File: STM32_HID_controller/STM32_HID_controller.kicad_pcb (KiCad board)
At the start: 2 copper layers, 237.3 x 103.7 mm, 49 parts, among them J1 USB_B_Micro, J2 Conn_01x04_Pin, J3 Conn_01x03_Pin, J5 Conn_01x03_Pin, SW1 SW_SPDT, SW10 SW_Push, SW11 SW_Push, SW14 SW_Push, SW2 SW_Push, SW3 SW_Push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

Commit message: final draft
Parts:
- added H7: MountingHole, MountingHole:MountingHole_2.2mm_M2, F.Cu at (108.0, 22.0)
- added H8: MountingHole, MountingHole:MountingHole_2.2mm_M2, F.Cu at (191.0, 22.0)
- moved H1 0.34 mm to (210.0, 22.0)
- moved H3 0.25 mm to (89.0, 22.0)
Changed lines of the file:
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@@
 		)
 	)
+	(footprint "MountingHole:MountingHole_2.2mm_M2"
+		(layer "F.Cu")
+		(at 108 22)
+		(descr "Mounting Hole 2.2mm, M2, no annular, generated by kicad-footprint-generator mountinghole.py")
+		(tags "mountinghole M2")
+		(property "Reference" "H7"
+			(at 0 -3.15 0)
+			(layer "F.SilkS")
+			(effects
+				(font
+					(size 1 1)
+					(thickness 0.15)
+				)
+			)
+		)
+		(property "Value" "MountingHole"
+			(at 0 3.15 0)
+			(layer "F.Fab")
+			(effects
+				(font
+					(size 1 1)
+					(thickness 0.15)
+				)
+			)
+		)
+		(property "Datasheet" "~"
+			(at 0 0 0)
+			(layer "F.Fab")
+			(hide yes)
+			(effects
+				(font
+					(size 1.27 1.27)
+					(thickness 0.15)
+				)
+			)
+		)
+		(property "Description" "Mounting Hole without connection"
+			(at 0 0 0)
+			(layer "F.Fab")
+			(hide yes)
+			(effects
+				(font
+					(size 1.27 1.27)
+					(thickness 0.15)
+				)
+			)
+		)
+		(property ki_fp_filters "MountingHole*")
+		(sheetname "/")
+		(sheetfile "STM32_HID_controller.kicad_sch")
+		(attr exclude_from_pos_files exclude_from_bom)
+		(fp_circle
+			(center 0 0)
+			(end 2.2 0)
+			(stroke
+				(width 0.15)
+				(type solid)
+			)
+			(fill no)
+			(layer "Cmts.User")
+		)
+		(fp_circle
+			(center 0 0)
+			(end 2.45 0)
+			(stroke
+				(width 0.05)
+				(type solid)
+			)
+			(fill no)
+			(layer "F.CrtYd")
+		)
+		(fp_text user "${REFERENCE}"
+			(at 0 0 0)
+			(layer "F.Fab")
+			(effects
+				(font
+					(size 1 1)
+					(thickness 0.15)
+				)
+			)
+		)
+		(pad "" np_thru_hole circle
+			(at 0 0)
+			(size 2.2 2.2)
+			(drill 2.2)
+			(layers "*.Cu" "*.Mask")
+		)
+		(embedded_fonts no)
+	)
 	(footprint "Capacitor_SMD:C_0402_1005Metric"
 		(layer "F.Cu")
@@
 		)
 	)
+	(footprint "MountingHole:MountingHole_2.2mm_M2"
+		(layer "F.Cu")
+		(at 191 22)
+		(descr "Mounting Hole 2.2mm, M2, no annular, generated by kicad-footprint-generator mountinghole.py")
+		(tags "mountinghole M2")
+		(property "Reference" "H8"
+			(at 0 -3.15 0)
+			(layer "F.SilkS")
+			(effects
+				(font
+					(size 1 1)
+					(thickness 0.15)
+				)
+			)
+		)
+		(property "Value" "MountingHole"
+			(at 0 3.15 0)
+			(layer "F.Fab")
+			(effects
+				(font
+					(size 1 1)
+					(thickness 0.15)
+				)
+			)
+		)
+		(property "Datasheet" "~"
+			(at 0 0 0)
+			(layer "F.Fab")
+			(hide yes)
+			(effects
+				(font
+					(size 1.27 1.27)
+					(thickness 0.15)
+				)
+			)
+		)
+		(property "Description" "Mounting Hole without connection"
+			(at 0 0 0)
+			(layer "F.Fab")
+			(hide yes)
+			(effects
+				(font
+					(size 1.27 1.27)
+					(thickness 0.15)
+				)
+			)
+		)
+		(property ki_fp_filters "MountingHole*")
+		(sheetname "/")
+		(sheetfile "STM32_HID_controller.kicad_sch")
+		(attr exclude_from_pos_files exclude_from_bom)
+		(fp_circle
+			(center 0 0)
+			(end 2.2 0)
+			(stroke
+				(width 0.15)
+				(type solid)
+			)
+			(fill no)
+			(layer "Cmts.User")
+		)
+		(fp_circle
+			(center 0 0)
+			(end 2.45 0)
+			(stroke
+				(width 0.05)
+				(type solid)
+			)
+			(fill no)
+			(layer "F.CrtYd")
+		)
+		(fp_text user "${REFERENCE}"
+			(at 0 0 0)
+			(layer "F.Fab")
+			(effects
+				(font
+					(size 1 1)
+					(thickness 0.15)
+				)
+			)
+		)
+		(pad "" np_thru_hole circle
+			(at 0 0)
+			(size 2.2 2.2)
+			(drill 2.2)
+			(layers "*.Cu" "*.Mask")
+		)
+		(embedded_fonts no)
+	)
 	(footprint "Inductor_SMD:L_0603_1608Metric"
 		(layer "F.Cu")
@@
 	(footprint "MountingHole:MountingHole_2.2mm_M2"
 		(layer "F.Cu")
-		(at 88.8 22.15)
+		(at 89 22)
 		(descr "Mounting Hole 2.2mm, M2, no annular, generated by kicad-footprint-generator mountinghole.py")
 		(tags "mountinghole M2")
@@
 	(footprint "MountingHole:MountingHole_2.2mm_M2"
 		(layer "F.Cu")
-		(at 210.3 22.15)
+		(at 210 22)
 		(descr "Mounting Hole 2.2mm, M2, no annular, generated by kicad-footprint-generator mountinghole.py")
 		(tags "mountinghole M2")

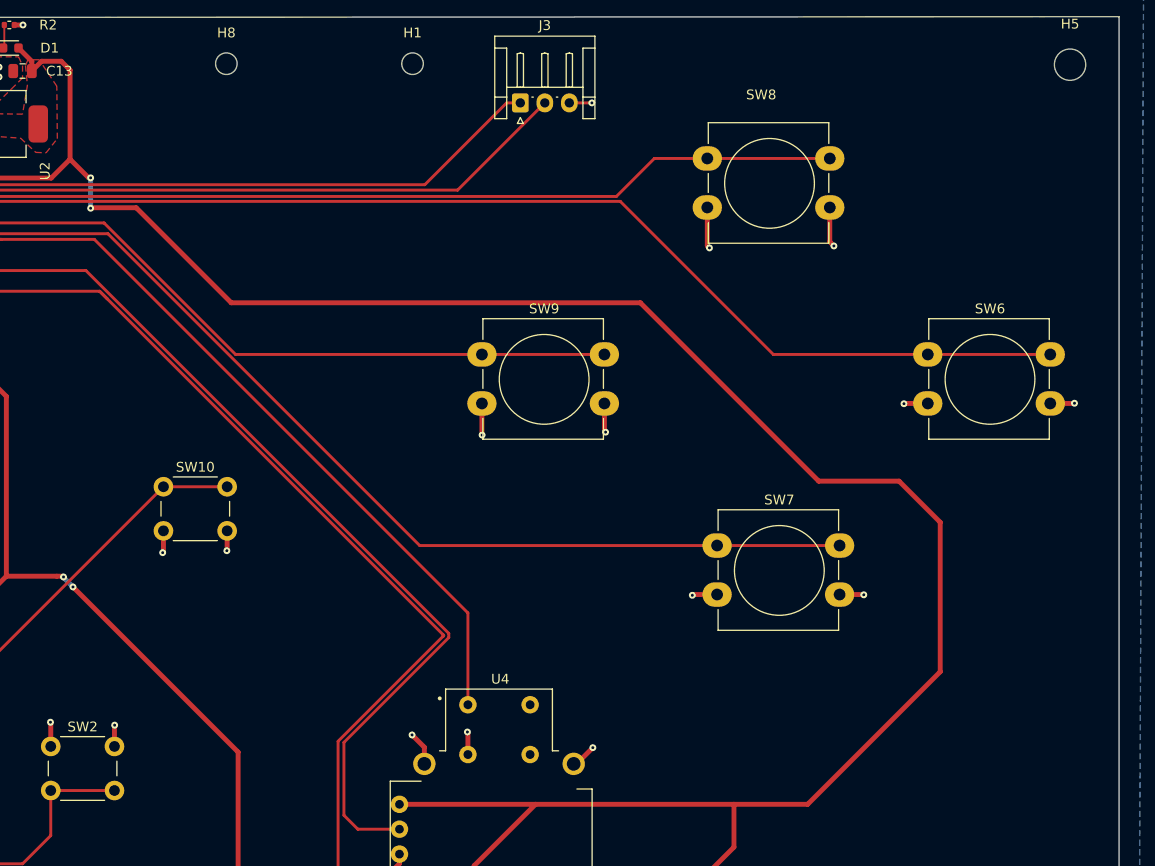
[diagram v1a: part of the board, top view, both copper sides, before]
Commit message: changed 3.3V mapping
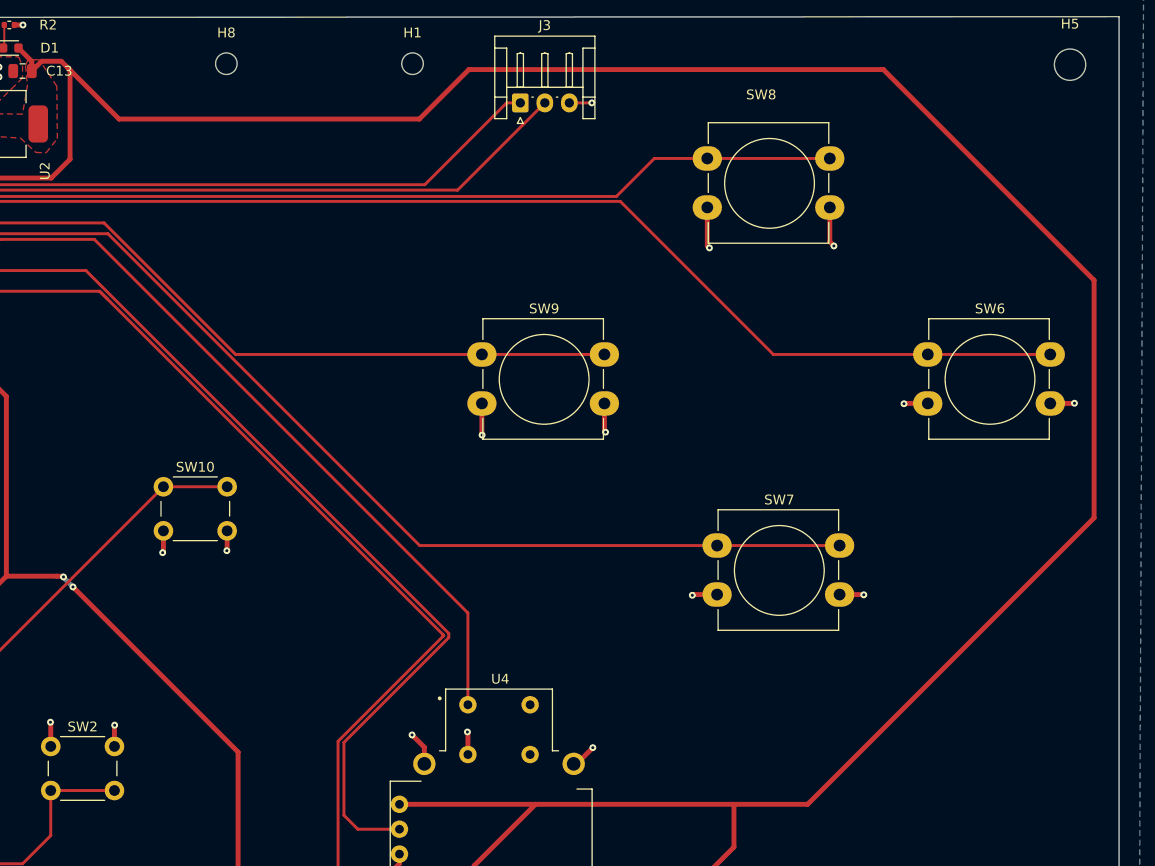
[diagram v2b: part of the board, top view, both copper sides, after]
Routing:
- net +3.3V: track 742.8 -> 785.9 mm, vias 18 -> 16

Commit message: added text
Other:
- board text added: "Bricked"
- board text added: "Flash"
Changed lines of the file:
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@@
 		(layer "Edge.Cuts")
+	)
+	(gr_text "Flash"
+		(at 129.35 34 0)
+		(layer "F.Cu")
+		(effects
+			(font
+				(size 0.6 0.6)
+				(thickness 0.15)
+				(bold yes)
+			)
+			(justify left bottom)
+		)
+	)
+	(gr_text "Bricked"
+		(at 128.8 40.8 0)
+		(layer "F.Cu")
+		(effects
+			(font
+				(size 0.6 0.6)
+				(thickness 0.15)
+				(bold yes)
+			)
+			(justify left bottom)
+		)
 	)
 	(segment

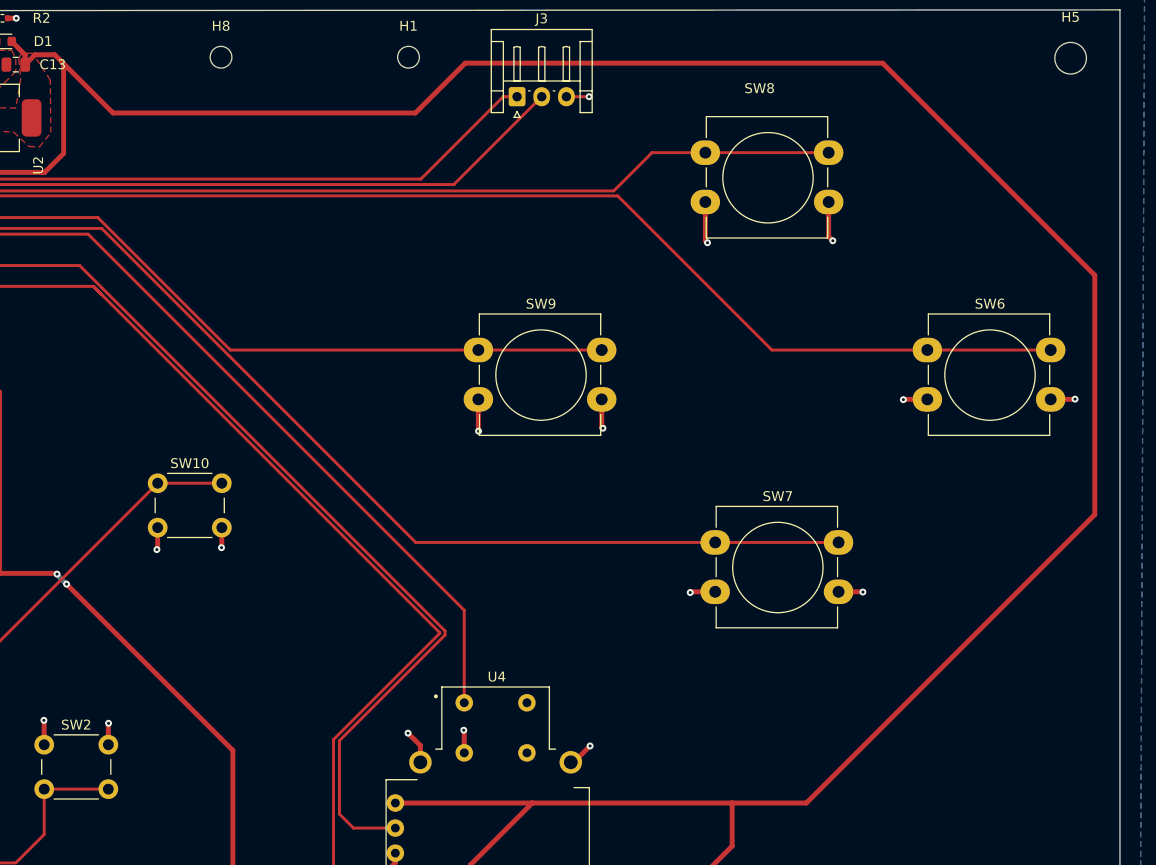
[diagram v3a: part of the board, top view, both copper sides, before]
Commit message: changed 3.3V routing
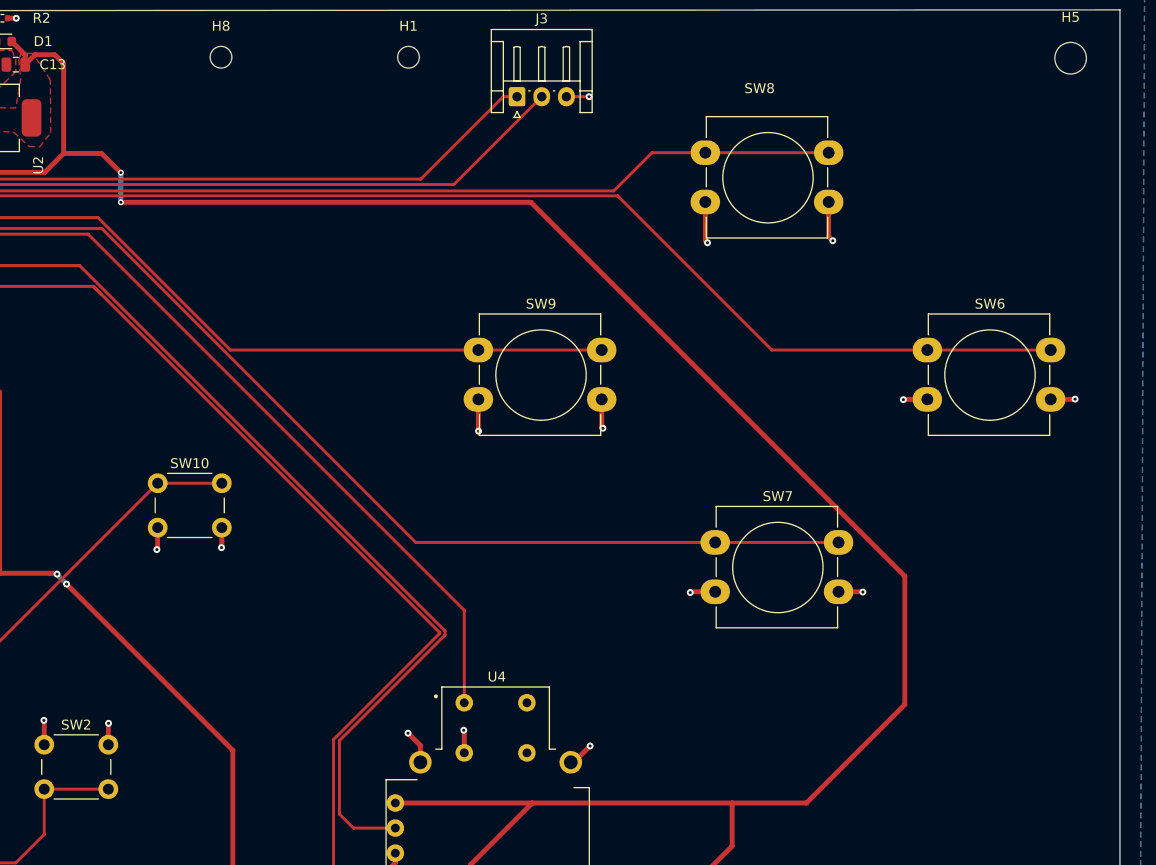
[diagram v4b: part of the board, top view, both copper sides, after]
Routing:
- net +3.3V: track 785.9 -> 734.3 mm, vias 16 -> 18
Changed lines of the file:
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@@
-	)
-	(segment
-		(start 279.55 44.1)
-		(end 279.55 68.35)
-		(width 0.5)
-		(layer "F.Cu")
-		(net 2)
 	)
 	(segment
@@
 	)
 	(segment
-		(start 210.7 27.65)
-		(end 215.75 22.6)
-		(width 0.5)
-		(layer "F.Cu")
-		(net 2)
-	)
-	(segment
 		(start 119.444975 58.055025)
 		(end 117.95 59.55)
@@
 	)
 	(segment
-		(start 215.75 22.6)
-		(end 258.05 22.6)
-		(width 0.5)
-		(layer "F.Cu")
-		(net 2)
-	)
-	(segment
-		(start 180.05 27.65)
-		(end 210.7 27.65)
-		(width 0.5)
-		(layer "F.Cu")
-		(net 2)
-	)
-	(segment
 		(start 192.2 92.25)
 		(end 192.2 104.75)
@@
 	)
 	(segment
+		(start 260.3 87.6)
+		(end 250.32 97.58)
+		(width 0.5)
+		(layer "F.Cu")
+		(net 2)
+	)
+	(segment
 		(start 124 59.5)
 		(end 124 59.45)
@@
 	)
 	(segment
-		(start 250.32 97.58)
-		(end 242.8 97.58)
-		(width 0.5)
-		(layer "F.Cu")
-		(net 2)
-	)
-	(segment
 		(start 84.2 42.3)
 		(end 66.12 60.38)
@@
 	)
 	(segment
+		(start 180.85 36.701)
+		(end 222.401 36.701)
+		(width 0.5)
+		(layer "F.Cu")
+		(net 2)
+	)
+	(segment
 		(start 56.3 65.05)
 		(end 56.3 64.75)
@@
 		(end 162.251 47.190364)
 		(width 0.3)
+		(layer "F.Cu")
+		(net 2)
+	)
+	(segment
+		(start 260.3 74.6)
+		(end 260.3 87.6)
+		(width 0.5)
 		(layer "F.Cu")
 		(net 2)
@@
 	)
 	(segment
-		(start 258.05 22.6)
-		(end 279.55 44.1)
-		(width 0.5)
-		(layer "F.Cu")
-		(net 2)
-	)
-	(segment
 		(start 56.125735 63.005025)
 		(end 58.75076 60.38)
@@
 		(start 110.55 59.55)
 		(end 110.15 59.15)
-		(width 0.5)
-		(layer "F.Cu")
-		(net 2)
-	)
-	(segment
-		(start 279.55 68.35)
-		(end 250.32 97.58)
 		(width 0.5)
 		(layer "F.Cu")
@@
 	)
 	(segment
+		(start 250.32 97.58)
+		(end 242.8 97.58)
+		(width 0.5)
+		(layer "F.Cu")
+		(net 2)
+	)
+	(segment
 		(start 147.53 45.83)
 		(end 147.735 46.035)
@@
 	)
 	(segment
-		(start 174.85 22.45)
-		(end 180.05 27.65)
-		(width 0.5)
-		(layer "F.Cu")
-		(net 2)
-	)
-	(segment
 		(start 175.33587 75.38587)
 		(end 192.2 92.25)
@@
 	)
 	(segment
+		(start 222.401 36.701)
+		(end 260.3 74.6)
+		(width 0.5)
+		(layer "F.Cu")
+		(net 2)
+	)
+	(segment
+		(start 178.9 31.75)
+		(end 180.85 33.7)
+		(width 0.5)
+		(layer "F.Cu")
+		(net 2)
+	)
+	(segment
 		(start 216.285 103.845)
 		(end 222.55 97.58)
@@
 	)
 	(segment
+		(start 175.05 31.75)
+		(end 178.9 31.75)
+		(width 0.5)
+		(layer "F.Cu")
+		(net 2)
+	)
+	(segment
 		(start 161.35 30.6)
 		(end 160.3 29.55)
@@
 	)
 	(via
+		(at 180.85 33.7)
+		(size 0.6)
+		(drill 0.3)
+		(layers "F.Cu" "B.Cu")
+		(net 2)
+	)
+	(via
 		(at 56.09038 62.96967)
 		(size 0.7)
@@
 		(at 122.555025 58.055025)
 		(size 0.7)
+		(drill 0.3)
+		(layers "F.Cu" "B.Cu")
+		(net 2)
+	)
+	(via
+		(at 180.85 36.701)
+		(size 0.6)
 		(drill 0.3)
 		(layers "F.Cu" "B.Cu")
@@
 		(width 0.5)
 		(layer "B.Cu")
+		(net 2)
+	)
+	(segment
+		(start 180.85 33.7)
+		(end 180.85 36.701)
+		(width 0.5)
+		(layer "B.Cu")
